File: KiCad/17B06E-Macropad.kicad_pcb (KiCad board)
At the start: 2 copper layers, 128.8 x 102.8 mm, 68 parts, among them SW1 RotaryEncoder_Switch, SW2 RotaryEncoder_Switch, SW3 RotaryEncoder_Switch, SW4 RotaryEncoder_Switch, SW5 RotaryEncoder_Switch, SW6 RotaryEncoder_Switch

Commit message: update
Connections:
- A1 pad 35: VCC -> unconnected-(A1-ADC_VREF-Pad35)
- A1 pad 40: /VBUS -> VCC +5V
- LED1 pad 1: VCC -> VCC +5V
- LED10 pad 1: VCC -> VCC +5V
- LED11 pad 1: VCC -> VCC +5V
- LED12 pad 1: VCC -> VCC +5V
- LED13 pad 1: VCC -> VCC +5V
- LED14 pad 1: VCC -> VCC +5V
- LED15 pad 1: VCC -> VCC +5V
- LED16 pad 1: VCC -> VCC +5V
- LED2 pad 1: VCC -> VCC +5V
- LED3 pad 1: VCC -> VCC +5V
- LED4 pad 1: VCC -> VCC +5V
- LED5 pad 1: VCC -> VCC +5V
- LED6 pad 1: VCC -> VCC +5V
- LED7 pad 1: VCC -> VCC +5V
- LED8 pad 1: VCC -> VCC +5V
- LED9 pad 1: VCC -> VCC +5V
- OLED1 pad 2: VCC -> VCC +5V
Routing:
- net VCC +5V: track 0.00 -> 419.8 mm, vias 0 -> 5
- net VCC: track 406.3 -> 0.00 mm, vias 5 -> 0
- net /ENCODER_L4: track 219.1 -> 217.3 mm

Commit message: Various adjustments/improvements
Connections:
- net /ENCODER_L1 renamed /ENCODER_L1a
- net /ENCODER_L2 renamed /ENCODER_L2b
- net /ENCODER_L3 renamed /ENCODER_L3b
- net /ENCODER_L4 renamed /ENCODER_L4a
- net /ENCODER_L6 renamed /ENCODER_L6a
- net /ENCODER_L7 renamed /ENCODER_L7b
- net /ENCODER_L8 renamed /ENCODER_L8b
- net /ENCODER_L9 renamed /ENCODER_L9b
- A1 pad 31: /ENCODER_L5 -> /ENCODER_L5b
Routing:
- net /COL2: track 179.6 -> 174.3 mm, vias 7 -> 6
- net /ROW0: track 117.0 -> 115.0 mm
- net /COL1: track 210.2 -> 208.4 mm
- net /COL4: track 262.5 -> 264.2 mm, vias 11 -> 9
- net /ROW3: track 132.9 -> 132.0 mm
- net /COL3: track 232.4 -> 233.3 mm, vias 11 -> 10
- net Net-(LED12-DOUT): track 23.5 -> 24.3 mm
- net /ROW5: track 166.1 -> 166.8 mm
- net /SCL: track 51.7 -> 52.3 mm
- net VCC +5V: track 419.8 -> 419.2 mm, vias 5 -> 4
- net /SDA: track 55.2 -> 55.8 mm
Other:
- board text added: "GND +5V SCL SDA"

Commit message: Encoder better labeled as a/b in the schematic
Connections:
- net /ENCODER_L1a renamed /ENCODER1u2_a
- net /ENCODER_L2b renamed /ENCODER1_b
- net /ENCODER_L3b renamed /ENCODER2_b
- net /ENCODER_L4a renamed /ENCODER3u6_a
- net /ENCODER_L6a renamed /ENCODER4u5_a
- net /ENCODER_L7b renamed /ENCODER4_b
- net /ENCODER_L8b renamed /ENCODER5_b
- net /ENCODER_L9b renamed /ENCODER6_b
- A1 pad 31: /ENCODER_L5b -> /ENCODER3_b
- SW3 pad B: /ENCODER_L5 -> /ENCODER3_b
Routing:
- net /ENCODER_L5: track 80.7 -> 0.00 mm
- net /ENCODER3_b: track 0.00 -> 80.7 mm

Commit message: various changes
holes changed, 
schematic correctly arranged,
and even more
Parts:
- added REF**: MountingHole_2.1mm, MountingHole:MountingHole_2.1mm, F.Cu at (108.5, 114.1)
- added REF**: MountingHole_2.1mm, MountingHole:MountingHole_2.1mm, F.Cu at (208.7, 74.5)
- added REF**: MountingHole_2.1mm, MountingHole:MountingHole_2.1mm, F.Cu at (208.7, 114.1)
- added REF**: MountingHole_2.1mm, MountingHole:MountingHole_2.1mm, F.Cu at (108.5, 74.5)
- moved REF** 1.31 mm to (177.7, 123.9)
- moved REF** 1.31 mm to (139.5, 123.9)
- moved REF** 1.31 mm to (177.7, 85.8)
- moved REF** 1.30 mm to (139.5, 85.8)
- moved D9 0.19 mm to (139.3, 113.1)
- moved D16 0.12 mm to (187.0, 124.5)
- moved D7 0.11 mm to (177.6, 93.9)
- moved D4 0.11 mm to (197.1, 75.1)
- moved D11 0.08 mm to (177.6, 113.0)
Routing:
- net /ENCODER3u6_a: track 217.3 -> 219.3 mm, vias 2 -> 1
- net /ROW0: track 115.0 -> 113.9 mm
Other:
- outline, holes or cut-outs redrawn
- board text added: "Simon99de x FabiClawZ"
- board text removed: "Simon99de"

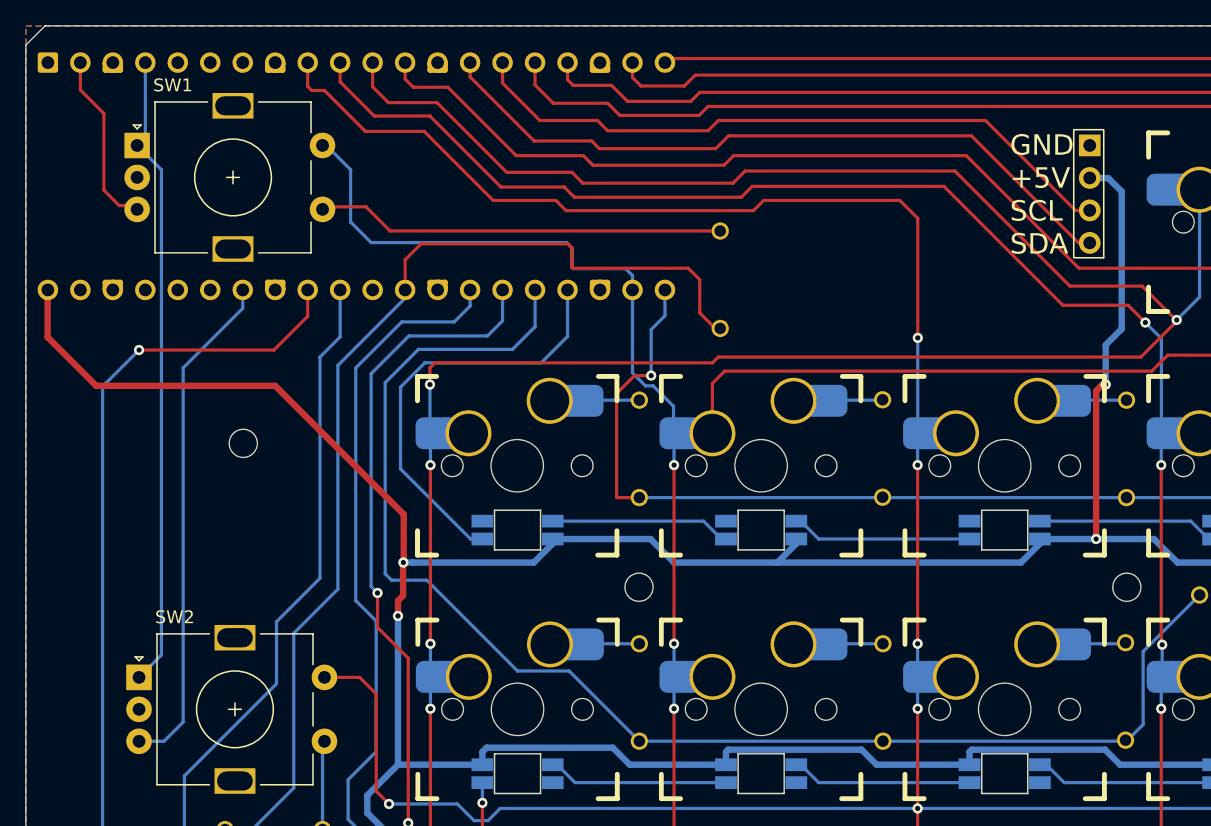
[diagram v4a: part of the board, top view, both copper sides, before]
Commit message: Pin description added for MCU
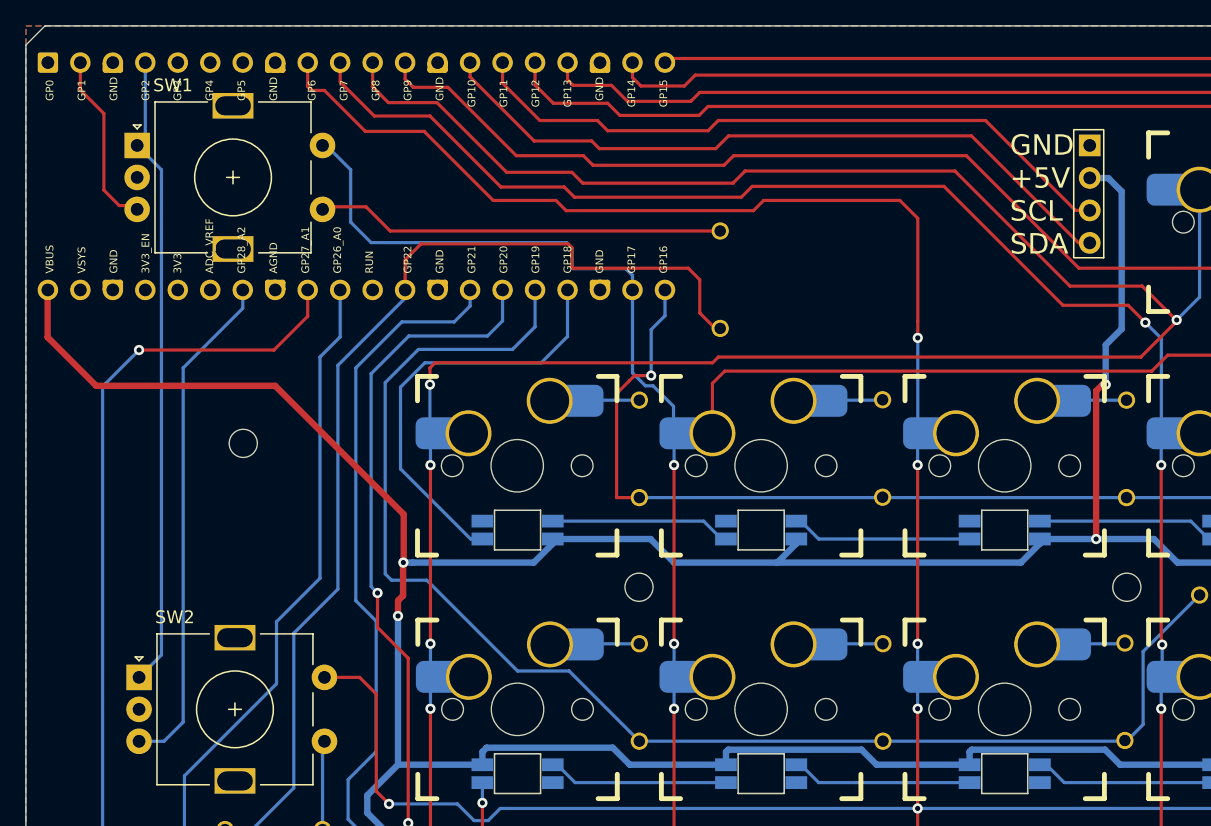
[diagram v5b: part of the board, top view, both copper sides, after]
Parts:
- moved D7 0.06 mm to (177.5, 93.9)
- renumbered A1 to MCU

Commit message: V1.0
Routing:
- net VCC +5V: track 419.0 -> 421.7 mm
- net /ROW3: track 132.0 -> 133.5 mm
- net Net-(LED4-DOUT): track 21.8 -> 23.0 mm
- net /ROW2: track 108.6 -> 109.3 mm
- net /ROW4: track 152.5 -> 153.0 mm
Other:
- board text added: "17B06E-Macropad - V1.0"
- board text added: "17B06E-Macropad - hotswap - rgb - OLED"
- board text removed: "17B06E-Macropad - hotswap - rgb"
